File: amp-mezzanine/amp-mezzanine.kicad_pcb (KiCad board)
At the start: 2 copper layers, 150 x 48 mm, 16 parts, among them J1 LOGIC_IN, J2 I2C, J3 PWR_A, J4 PWR_B

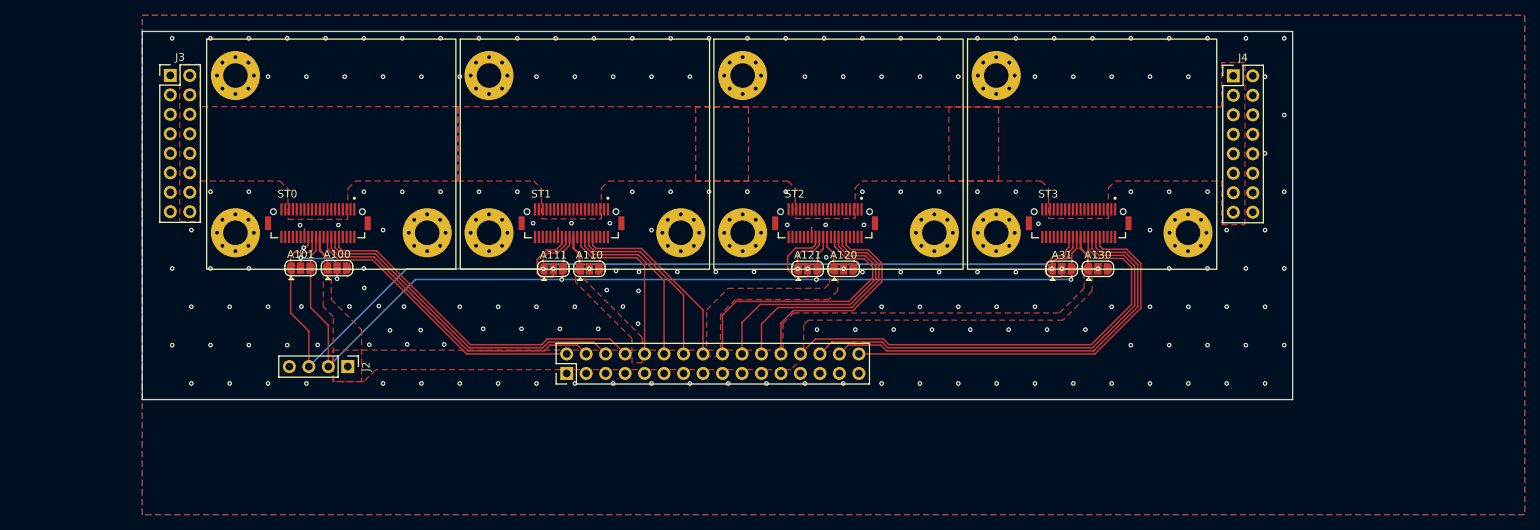
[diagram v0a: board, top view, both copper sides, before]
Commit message: Added DS2484 to mezzanine board
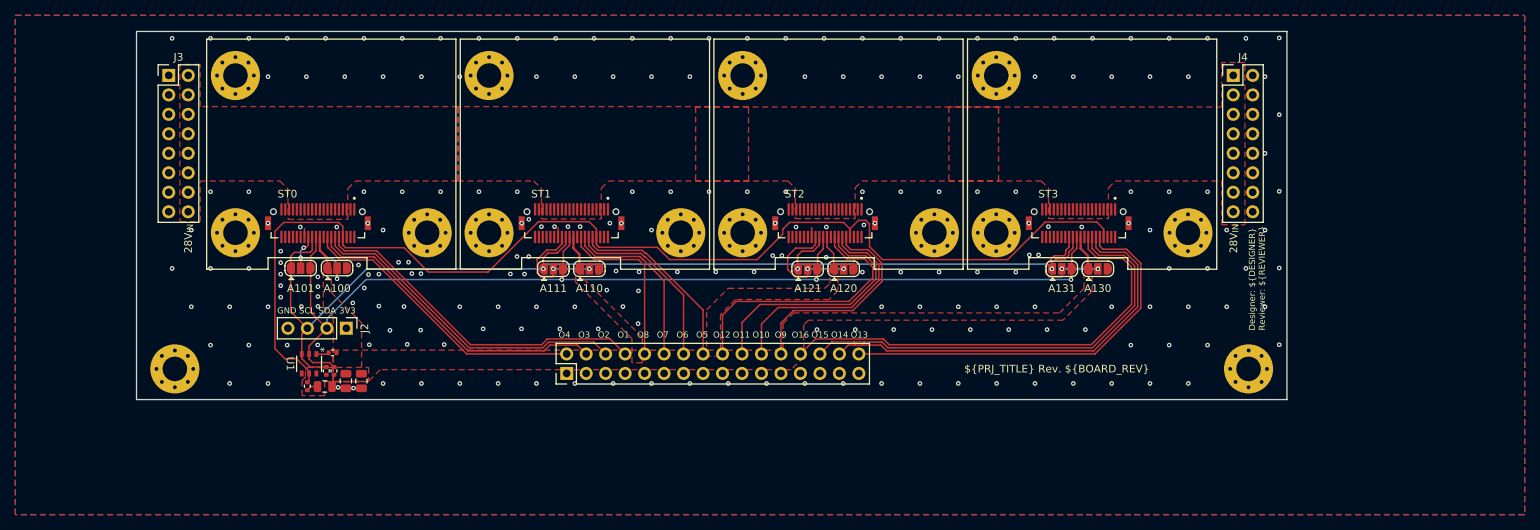
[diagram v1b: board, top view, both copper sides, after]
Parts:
- added C1: 10u, Capacitor_SMD:C_0805_2012Metric, F.Cu at (96.5, 97.6)
- added C2: 10u, Capacitor_SMD:C_0805_2012Metric, F.Cu at (98.6, 97.6)
- added C3: 0.1u, Capacitor_SMD:C_0805_2012Metric, F.Cu at (93.8, 98.3)
- added H1: MountingHole_Pad, MountingHole:MountingHole_3.2mm_M3_Pad_Via, F.Cu at (74.2, 96.0)
- added H2: MountingHole_Pad, MountingHole:MountingHole_3.2mm_M3_Pad_Via, F.Cu at (214.2, 96.0)
- added R1: 10k, Resistor_SMD:R_0402_1005Metric, F.Cu at (94.0, 96.3)
- added R2: 10k, Resistor_SMD:R_0402_1005Metric, F.Cu at (95.0, 96.3)
- added R3: 1k, Resistor_SMD:R_0402_1005Metric, F.Cu at (91.5, 98.3)
- added R4: 2.2k, Resistor_SMD:R_0402_1005Metric, F.Cu at (94.8, 93.9)
- added U1: DS2484R+T, project_footprints:21-0058I_MXM-L, F.Cu at (91.7, 95.3)
- A100: value GND -> R
- A110: value 3V3 -> L
- A121: value SDA -> R
- A131: renamed from A31; value SCL -> L
- ST0: value STACK_0 -> PICD-DAC-STACK
- ST1: value STACK_1 -> PICD-DAC-STACK
- ST2: value STACK_2 -> PICD-DAC-STACK
- ST3: value STACK_3 -> PICD-DAC-STACK
- moved J2 5.00 mm to (96.6, 90.7)
- moved J3 0.21 mm to (73.5, 57.7)
- moved J4 0.06 mm to (212.2, 57.7)
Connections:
- ST0 pad 37: GND -> /ONEWIRE
- ST1 pad 37: GND -> /ONEWIRE
- ST2 pad 37: GND -> /ONEWIRE
- ST3 pad 37: GND -> /ONEWIRE
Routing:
- net /ONEWIRE: track 0.00 -> 152.7 mm
- net /SDA: track 136.7 -> 139.1 mm
- net Net-(U1-SLPZ): track 0.00 -> 1.67 mm
- net +3V3: track 17.2 -> 18.7 mm
- net /SCL: track 140.9 -> 141.8 mm
- net GND: vias 190 -> 219
- net (no net): vias 0 -> 2
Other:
- board text added: "${PRJ_TITLE} Rev. ${BOARD_REV}"
- board text added: "28V_{IN}"
- board text added: "3V3"
- board text added: "Designer: ${DESIGNER} Reviewer: ${REVIEWER}"
- board text added: "GND"
- board text added: "O1"
- board text added: "O10"
- board text added: "O11"
- board text added: "O12"
- board text added: "O13"
- board text added: "O14"
- board text added: "O15"
- board text added: "O16"
- board text added: "O2"
- board text added: "O3"
- board text added: "O4"
- board text added: "O5"
- board text added: "O6"
- board text added: "O7"
- board text added: "O8"
- board text added: "O9"
- board text added: "SCL"
- board text added: "SDA"

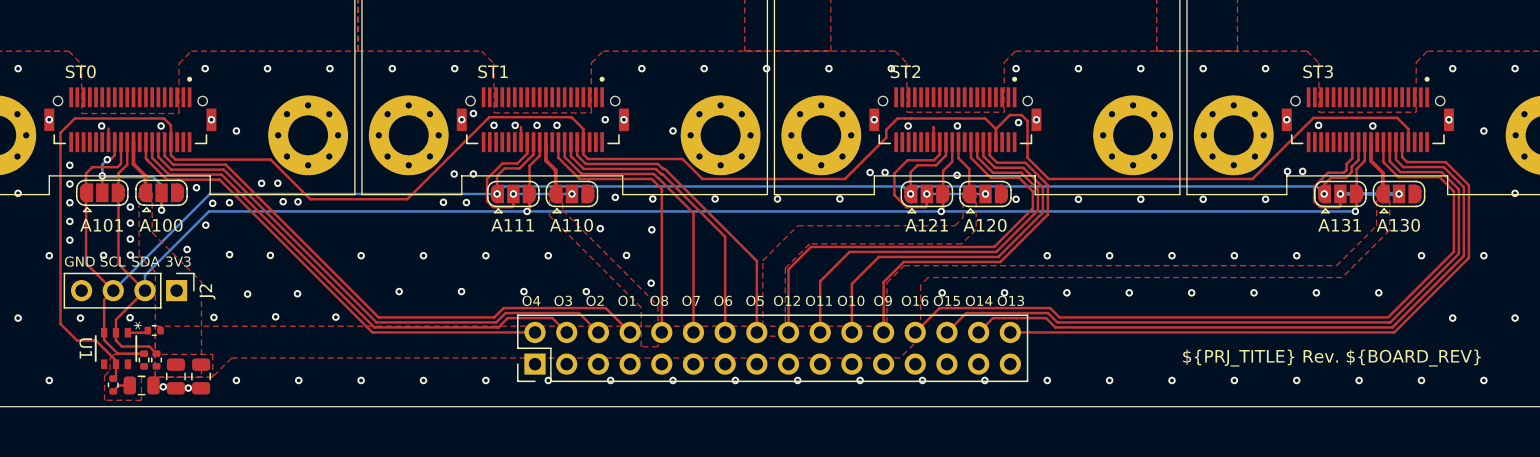
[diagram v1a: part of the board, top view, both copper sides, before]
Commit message: Modified DAC, AMP v2 and Mezzanine to support AMP v3. Finished AMP v3 design.
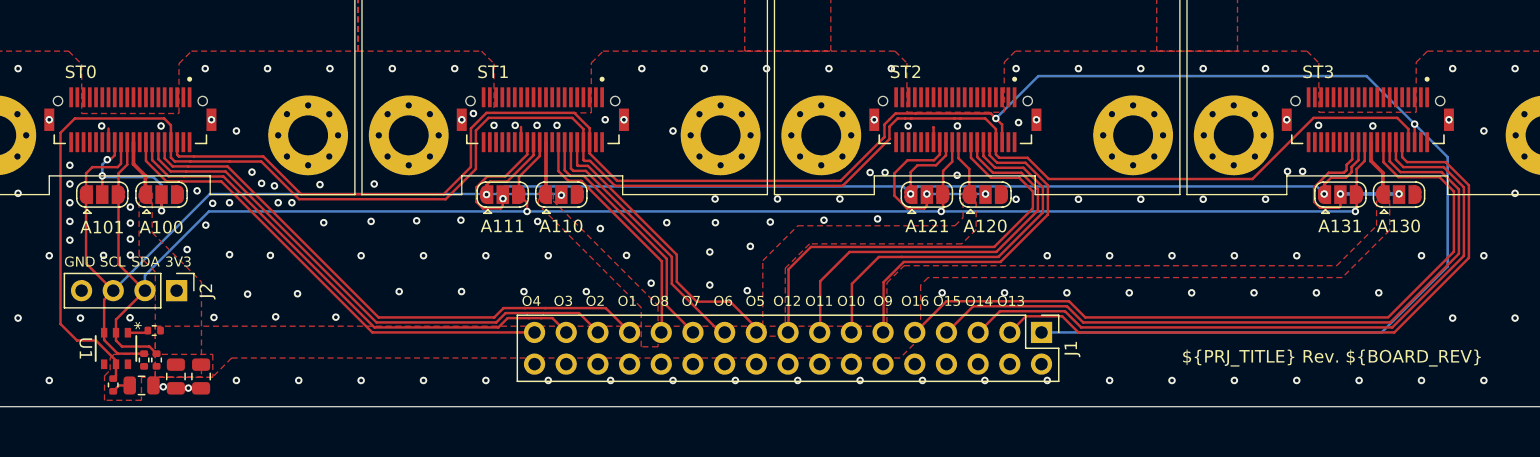
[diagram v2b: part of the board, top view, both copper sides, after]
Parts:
- J1: footprint Connector_PinHeader_2.54mm:PinHeader_2x16_P2.54mm_Vertical -> Connector_PinHeader_2.54mm:PinHeader_2x17_P2.54mm_Vertical
- moved J1 40.7 mm to (165.9, 94.0), turned to -90 degrees
- moved A110 0.85 mm to (127.5, 83.0)
- moved A111 0.85 mm to (122.8, 83.0)
- moved A100 0.14 mm to (95.4, 83.0)
- moved A101 0.14 mm to (90.7, 83.0)
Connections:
- J1 pad 1: GND -> /EN
- J1 pad 10: /CTRL_D1 -> GND
- J1 pad 11: GND -> /CTRL_A2
- J1 pad 12: /CTRL_C1 -> GND
- J1 pad 13: GND -> /CTRL_B2
- J1 pad 14: /CTRL_B1 -> GND
- J1 pad 15: GND -> /CTRL_C2
- J1 pad 16: /CTRL_A1 -> GND
- J1 pad 17: GND -> /CTRL_D2
- J1 pad 18: /CTRL_D2 -> GND
- J1 pad 19: GND -> /CTRL_A1
- J1 pad 2: /CTRL_D0 -> GND
- J1 pad 20: /CTRL_C2 -> GND
- J1 pad 21: GND -> /CTRL_B1
- J1 pad 22: /CTRL_B2 -> GND
- J1 pad 23: GND -> /CTRL_C1
- J1 pad 24: /CTRL_A2 -> GND
- J1 pad 25: GND -> /CTRL_D1
- J1 pad 26: /CTRL_D3 -> GND
- J1 pad 27: GND -> /CTRL_A0
- J1 pad 28: /CTRL_C3 -> GND
- J1 pad 29: GND -> /CTRL_B0
- J1 pad 3: GND -> /CTRL_A3
- J1 pad 30: /CTRL_B3 -> GND
- J1 pad 31: GND -> /CTRL_C0
- J1 pad 32: /CTRL_A3 -> GND
- J1 pad 4: /CTRL_C0 -> GND
- J1 pad 5: GND -> /CTRL_B3
- J1 pad 6: /CTRL_B0 -> GND
- J1 pad 7: GND -> /CTRL_C3
- J1 pad 8: /CTRL_A0 -> GND
- J1 pad 9: GND -> /CTRL_D3
- ST0 pad 38: GND -> /EN
- ST1 pad 38: GND -> /EN
- ST2 pad 38: GND -> /EN
- ST3 pad 38: GND -> /EN
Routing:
- net /EN: track 0.00 -> 166.3 mm, vias 0 -> 2
- net /CTRL_C1: track 22.9 -> 20.2 mm
- net /CTRL_D1: track 22.1 -> 19.3 mm
- net /CTRL_B1: track 23.8 -> 21.2 mm
- net /SDA: track 139.1 -> 140.5 mm
- net /CTRL_A1: track 24.7 -> 23.3 mm
- net /SCL: track 141.8 -> 143.2 mm
- net /CTRL_A3: track 52.5 -> 53.7 mm
- net /A1_1: track 14.8 -> 15.5 mm
- net +3V3: track 18.7 -> 19.4 mm
- net GND: vias 219 -> 229
